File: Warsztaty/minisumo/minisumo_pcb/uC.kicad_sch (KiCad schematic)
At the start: 10 parts, among them U4 ATMEGA328P-AU

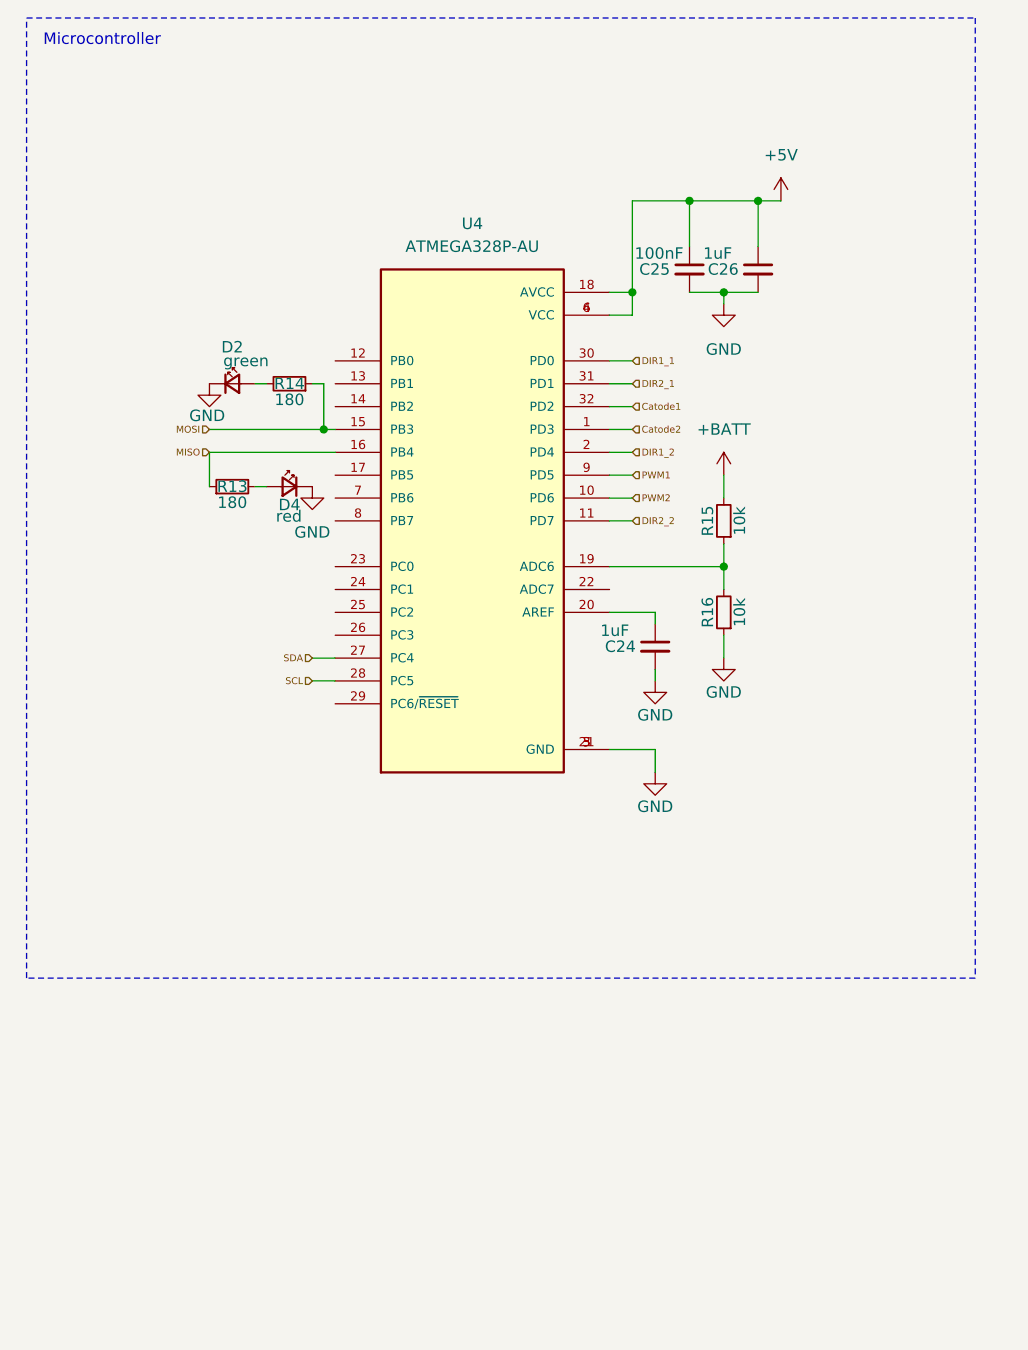
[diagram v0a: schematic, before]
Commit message: laczenie hierarchiczne schematu
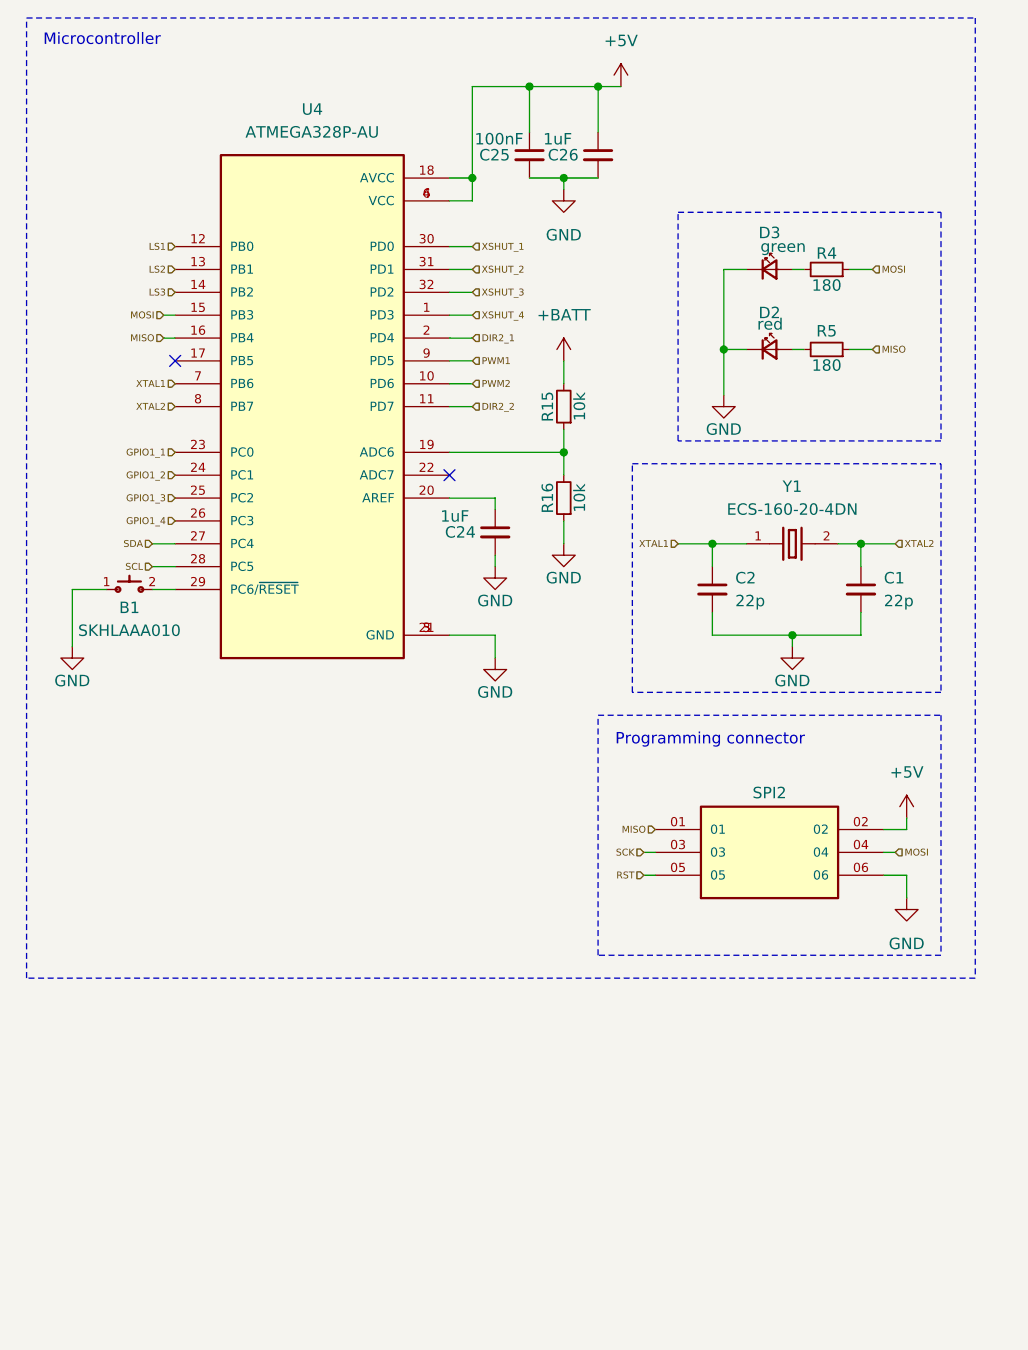
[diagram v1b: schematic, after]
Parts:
- removed D4: red, symbol Device:LED_Small
- removed R13, R14: 180, symbol Device:R_Small
- added B1: SKHLAAA010, SKHLAAA010:SKHLAAA010, symbol SKHLAAA010:SKHLAAA010
- added C1, C2: 22p, symbol Device:C_Small
- added D3: green, symbol Device:LED_Small
- added R4, R5: 180, symbol Device:R_Small
- added SPI2: MTSW-103-23-F-D-230, MTSW-103-23-F-D-230:SAMTEC_MTSW-103-23-F-D-230, symbol MTSW-103-23-F-D-230:MTSW-103-23-F-D-230
- added Y1: ECS-160-20-4DN, ECS-160-20-4DN:XTAL_ECS-160-20-4DN, symbol ECS-160-20-4DN:ECS-160-20-4DN
- D2: value green -> red
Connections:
- net DIR1_2 is gone; now on net DIR2_1: U4.2 (PD4)
- net +5V: now also SPI2.02
- net DIR2_1: no longer U4.31 (PD1)
- net GND: now also B1.1, C1.2, C2.2, D3.1 (K), SPI2.06
- net MISO: now also R5.1, SPI2.01
- net MOSI: now also R4.1, SPI2.04
- net LS1: now reaches U4.12 (PB0)
- net LS2: now reaches U4.13 (PB1)
- net LS3: now reaches U4.14 (PB2)
- net GPIO1_1: now reaches U4.23 (PC0)
- net GPIO1_2: now reaches U4.24 (PC1)
- net GPIO1_3: now reaches U4.25 (PC2)
- net GPIO1_4: now reaches U4.26 (PC3)
- net at U4.29 (PC6/~{RESET}): now also B1.2
- net XTAL1: now reaches U4.7 (PB6)
- net XTAL1: now also C2.1, Y1.1
- net XTAL2: now reaches U4.8 (PB7)
- net XTAL2: now also C1.1, Y1.2
- net at D2.2 (A): now also R5.2
- net Catode1 renamed XSHUT_3
- net Catode2 renamed XSHUT_4
- net DIR1_1 renamed XSHUT_1
- new net: D3.2 (A), R4.2
- new net RST: SPI2.05
- new net SCK: SPI2.03
- new net XSHUT_2: U4.31 (PD1)
- no-connect marks 0 -> 2
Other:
- note added: "Programming connector"
- moved on the sheet: C24, C25, C26, R15, R16, U4

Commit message: wstepnie skonczony schemat
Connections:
- net DIR2_1 renamed DIR1_2
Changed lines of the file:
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@@
 		)
 	)
-	(hierarchical_label "DIR2_1"
+	(hierarchical_label "DIR1_2"
 		(shape input)
 		(at 64.77 50.8 0)

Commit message: chyba gotowy schemat
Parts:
- removed SPI2: MTSW-103-23-F-D-230, MTSW-103-23-F-D-230:SAMTEC_MTSW-103-23-F-D-230, symbol MTSW-103-23-F-D-230:MTSW-103-23-F-D-230
- added SENS1, SENS2, SENS3, SENS4: MTSW-103-23-F-D-230, MTSW-103-23-F-D-230:SAMTEC_MTSW-103-23-F-D-230, symbol MTSW-103-23-F-D-230:MTSW-103-23-F-D-230
- C1, C2, C24, C25, C26: footprint (none) -> Capacitor_SMD:C_0805_2012Metric_Pad1.18x1.45mm_HandSolder
- D2, D3: footprint (none) -> LED_THT:LED_D3.0mm
- R15, R16, R4, R5: footprint (none) -> Resistor_SMD:R_0805_2012Metric_Pad1.20x1.40mm_HandSolder
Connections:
- net GND: now also SENS1.01, SENS2.01, SENS3.01, SENS4.01
- net GPIO1_1: now also SENS1.03
- net GPIO1_2: now also SENS2.03
- net GPIO1_3: now also SENS3.03
- net GPIO1_4: now also SENS4.03
- net SCL: now also SENS1.05, SENS2.05, SENS3.05, SENS4.05
- net SDA: now also SENS1.06, SENS2.06, SENS3.06, SENS4.06
- net XSHUT_1: now also SENS1.04
- net XSHUT_2: now also SENS2.04
- net XSHUT_3: now also SENS3.04
- net XSHUT_4: now also SENS4.04
- new net +3V3: SENS1.02, SENS2.02, SENS3.02, SENS4.02
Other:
- note removed: "Programming connector"

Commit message: chyba gotowy schemat
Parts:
- removed SENS1, SENS2, SENS3, SENS4: MTSW-103-23-F-D-230, MTSW-103-23-F-D-230:SAMTEC_MTSW-103-23-F-D-230, symbol MTSW-103-23-F-D-230:MTSW-103-23-F-D-230
- added C18: 100nF, Capacitor_SMD:C_0805_2012Metric_Pad1.18x1.45mm_HandSolder, symbol Device:C_Small
- added R47: 10k, Resistor_SMD:R_0805_2012Metric_Pad1.20x1.40mm_HandSolder, symbol Device:R_Small
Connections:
- net +5V: now also C18.1, R47.2
- net GND: now also C18.2
- net GPIO1_1: now also U4.12 (PB0); no longer U4.23 (PC0)
- net GPIO1_2: now also U4.13 (PB1); no longer U4.24 (PC1)
- net GPIO1_3: now also U4.14 (PB2); no longer U4.25 (PC2)
- net LS1: now also U4.23 (PC0); no longer U4.12 (PB0)
- net LS2: now also U4.24 (PC1); no longer U4.13 (PB1)
- net LS3: now also U4.25 (PC2); no longer U4.14 (PB2)
- net SCK: now reaches U4.17 (PB5)
- net RST: now reaches B1.2, U4.29 (PC6/~{RESET})
- net RST: now also R47.1
- net DIR1_2 renamed DIRB_1
- net DIR2_2 renamed DIRB_2
- no-connect marks 2 -> 1
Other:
- moved on the sheet: B1, C1, C2, C24, C25, C26, D2, D3, R15, R16, R4, R5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

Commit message: stan przed usunięciem jednego czujnika lini
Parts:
- C1, C18, C2, C24, C25, C26: footprint Capacitor_SMD:C_0805_2012Metric_Pad1.18x1.45mm_HandSolder -> Capacitor_SMD:C_0805_2012Metric
- R15, R16, R4, R5: footprint Resistor_SMD:R_0805_2012Metric_Pad1.20x1.40mm_HandSolder -> Resistor_SMD:R_0805_2012Metric
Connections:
- net LS3: no longer names the net of U4.25 (PC2)
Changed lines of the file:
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@@
-		)
-	)
-	(hierarchical_label "LS3"
-		(shape input)
-		(at 50.8 68.58 180)
-		(fields_autoplaced yes)
-		(effects
-			(font
-				(size 0.762 0.762)
-			)
-			(justify right)
 		)
 	)
@@
 			)
 		)
-		(property "Footprint" "Capacitor_SMD:C_0805_2012Metric_Pad1.18x1.45mm_HandSolder"
+		(property "Footprint" "Capacitor_SMD:C_0805_2012Metric"
 			(at 59.69 107.95 0)
 			(effects
@@
 			)
 		)
-		(property "Footprint" "Resistor_SMD:R_0805_2012Metric_Pad1.20x1.40mm_HandSolder"
+		(property "Footprint" "Resistor_SMD:R_0805_2012Metric"
 			(at 93.98 68.58 0)
 			(effects
@@
 			)
 		)
-		(property "Footprint" "Capacitor_SMD:C_0805_2012Metric_Pad1.18x1.45mm_HandSolder"
+		(property "Footprint" "Capacitor_SMD:C_0805_2012Metric"
 			(at 90.17 30.48 0)
 			(effects
@@
 			)
 		)
-		(property "Footprint" "Resistor_SMD:R_0805_2012Metric_Pad1.20x1.40mm_HandSolder"
+		(property "Footprint" "Resistor_SMD:R_0805_2012Metric"
 			(at 93.98 58.42 0)
 			(effects
@@
 			)
 		)
-		(property "Footprint" "Capacitor_SMD:C_0805_2012Metric_Pad1.18x1.45mm_HandSolder"
+		(property "Footprint" "Capacitor_SMD:C_0805_2012Metric"
 			(at 76.2 107.95 0)
 			(effects
@@
 			)
 		)
-		(property "Footprint" "Capacitor_SMD:C_0805_2012Metric_Pad1.18x1.45mm_HandSolder"
+		(property "Footprint" "Capacitor_SMD:C_0805_2012Metric"
 			(at 97.79 30.48 0)
 			(effects
@@
 			)
 		)
-		(property "Footprint" "Capacitor_SMD:C_0805_2012Metric_Pad1.18x1.45mm_HandSolder"
+		(property "Footprint" "Capacitor_SMD:C_0805_2012Metric"
 			(at 86.36 72.39 0)
 			(effects
@@
 			)
 		)
-		(property "Footprint" "Resistor_SMD:R_0805_2012Metric_Pad1.20x1.40mm_HandSolder"
+		(property "Footprint" "Resistor_SMD:R_0805_2012Metric"
 			(at 34.29 109.22 0)
 			(effects
@@
 			)
 		)
-		(property "Footprint" "Resistor_SMD:R_0805_2012Metric_Pad1.20x1.40mm_HandSolder"
+		(property "Footprint" "Resistor_SMD:R_0805_2012Metric"
 			(at 34.29 100.33 0)
 			(effects
@@
 			)
 		)
-		(property "Footprint" "Capacitor_SMD:C_0805_2012Metric_Pad1.18x1.45mm_HandSolder"
+		(property "Footprint" "Capacitor_SMD:C_0805_2012Metric"
 			(at 31.75 69.85 0)
 			(effects

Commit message: Wstępny wyglad robota i płytki
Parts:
- added J2: MTSW-103-23-F-S-235, MTSW-103-23-F-S-235:SAMTEC_MTSW-103-23-F-S-235, symbol MTSW-103-23-F-S-235:MTSW-103-23-F-S-235
- D2, D3: footprint LED_THT:LED_D3.0mm -> LED_SMD:LED_0805_2012Metric
- R4, R5: value 180 -> 1k
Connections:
- net +5V: now also J2.01
- net GND: now also J2.02
- net LS3: now reaches U4.25 (PC2)
- net GPIO1_1: no longer names the net of U4.12 (PB0)
- net GPIO1_2: no longer names the net of U4.13 (PB1)
- net GPIO1_3: no longer names the net of U4.14 (PB2)
- net GPIO1_4 renamed STARTER
- net STARTER: now also J2.03
- no-connect marks 1 -> 4
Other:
- note added: "Starter connector"

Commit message: koncowy projekt plytki i chyba model tez
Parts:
- renumbered D2 to MISO1, D3 to MOSI1, U4 to uC1
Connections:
- net LS1: now also uC1.25 (PC2); no longer uC1.23 (PC0)
- net LS3: now also uC1.23 (PC0); no longer uC1.25 (PC2)
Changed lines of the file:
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@@
 		)
 	)
-	(hierarchical_label "LS1"
+	(hierarchical_label "LS3"
 		(shape input)
 		(at 50.8 63.5 180)
@@
 		)
 	)
-	(hierarchical_label "LS3"
+	(hierarchical_label "LS1"
 		(shape input)
 		(at 50.8 68.58 180)
@@
 		(dnp no)
 		(fields_autoplaced yes)
-		(property "Reference" "U4"
+		(property "Reference" "uC1"
 			(at 66.04 25.4 0)
 			(effects
@@
 			(project "minisumo_pcb"
 				(path "/7b99a4ad-c15f-48f5-acdf-b2b295c8ee3b/2841fc75-29f5-4e06-b481-1d26a5df72c5"
-					(reference "U4")
+					(reference "uC1")
 					(unit 1)
 				)
@@
 		(on_board yes)
 		(dnp no)
-		(property "Reference" "D3"
+		(property "Reference" "MOSI1"
 			(at 27.94 96.266 0)
 			(effects
@@
 			(project "minisumo_pcb"
 				(path "/7b99a4ad-c15f-48f5-acdf-b2b295c8ee3b/2841fc75-29f5-4e06-b481-1d26a5df72c5"
-					(reference "D3")
+					(reference "MOSI1")
 					(unit 1)
 				)
@@
 		(on_board yes)
 		(dnp no)
-		(property "Reference" "D2"
+		(property "Reference" "MISO1"
 			(at 27.94 105.156 0)
 			(effects
@@
 			(project "minisumo_pcb"
 				(path "/7b99a4ad-c15f-48f5-acdf-b2b295c8ee3b/2841fc75-29f5-4e06-b481-1d26a5df72c5"
-					(reference "D2")
-					(unit 1)
-				)
+					(reference "MISO1")
+					(unit 1)
+				)

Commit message: prawdopodobnie koncowa wersja płytki
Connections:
- net DIRB_2: now also uC1.12 (PB0); no longer uC1.11 (PD7)
- net LS1: now also uC1.23 (PC0); no longer uC1.25 (PC2)
- net LS2: now also uC1.25 (PC2); no longer uC1.24 (PC1)
- net LS3: now also uC1.24 (PC1); no longer uC1.23 (PC0)
- net PWM1: now also uC1.13 (PB1); no longer uC1.9 (PD5)
- net PWM2: now also uC1.14 (PB2); no longer uC1.10 (PD6)
- net XSHUT_1: now also uC1.1 (PD3); no longer uC1.30 (PD0)
- net XSHUT_2: now also uC1.32 (PD2); no longer uC1.31 (PD1)
- net XSHUT_3: now also uC1.31 (PD1); no longer uC1.32 (PD2)
- net XSHUT_4: now also uC1.30 (PD0); no longer uC1.1 (PD3)
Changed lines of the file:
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@@
 	)
 	(no_connect
-		(at 50.8 43.18)
+		(at 83.82 55.88)
 	)
 	(no_connect
-		(at 50.8 45.72)
+		(at 83.82 58.42)
 	)
 	(no_connect
@@
 	)
 	(no_connect
-		(at 50.8 40.64)
+		(at 83.82 53.34)
 	)
 	(wire
@@
 	(wire
 		(pts
+			(xy 49.53 43.18) (xy 50.8 43.18)
+		)
+		(stroke
+			(width 0)
+			(type default)
+		)
+	)
+	(wire
+		(pts
 			(xy 93.98 60.96) (xy 93.98 63.5)
 		)
@@
 	(wire
 		(pts
+			(xy 49.53 45.72) (xy 50.8 45.72)
+		)
+		(stroke
+			(width 0)
+			(type default)
+		)
+	)
+	(wire
+		(pts
 			(xy 81.28 33.02) (xy 83.82 33.02)
 		)
@@
 	(wire
 		(pts
+			(xy 49.53 40.64) (xy 50.8 40.64)
+		)
+		(stroke
+			(width 0)
+			(type default)
+		)
+	)
+	(wire
+		(pts
 			(xy 86.36 68.58) (xy 86.36 69.85)
 		)
@@
 		)
 	)
-	(hierarchical_label "DIRB_2"
+	(hierarchical_label "RST"
 		(shape input)
-		(at 83.82 58.42 0)
+		(at 29.21 78.74 180)
 		(fields_autoplaced yes)
 		(effects
@@
 				(size 0.762 0.762)
 			)
-			(justify left)
+			(justify right)
 		)
 	)
-	(hierarchical_label "RST"
+	(hierarchical_label "XSHUT_4"
 		(shape input)
-		(at 29.21 78.74 180)
+		(at 83.82 40.64 0)
 		(fields_autoplaced yes)
 		(effects
@@
 				(size 0.762 0.762)
 			)
-			(justify right)
+			(justify left)
 		)
 	)
-	(hierarchical_label "LS2"
+	(hierarchical_label "MOSI"
 		(shape input)
-		(at 50.8 66.04 180)
+		(at 39.37 100.33 0)
 		(fields_autoplaced yes)
 		(effects
@@
 				(size 0.762 0.762)
 			)
-			(justify right)
+			(justify left)
 		)
 	)
-	(hierarchical_label "PWM1"
+	(hierarchical_label "XSHUT_2"
 		(shape input)
-		(at 83.82 53.34 0)
+		(at 83.82 45.72 0)
 		(fields_autoplaced yes)
 		(effects
@@
 		)
 	)
-	(hierarchical_label "MOSI"
+	(hierarchical_label "SCK"
 		(shape input)
-		(at 39.37 100.33 0)
+		(at 50.8 53.34 180)
 		(fields_autoplaced yes)
 		(effects
@@
 				(size 0.762 0.762)
 			)
-			(justify left)
+			(justify right)
 		)
 	)
-	(hierarchical_label "XSHUT_3"
+	(hierarchical_label "MISO"
 		(shape input)
-		(at 83.82 45.72 0)
+		(at 39.37 109.22 0)
 		(fields_autoplaced yes)
 		(effects
@@
 		)
 	)
-	(hierarchical_label "PWM2"
+	(hierarchical_label "XSHUT_1"
 		(shape input)
-		(at 83.82 55.88 0)
+		(at 83.82 48.26 0)
 		(fields_autoplaced yes)
 		(effects
@@
 		)
 	)
-	(hierarchical_label "SCK"
+	(hierarchical_label "PWM2"
 		(shape input)
-		(at 50.8 53.34 180)
+		(at 49.53 45.72 180)
 		(fields_autoplaced yes)
 		(effects
@@
 		)
 	)
-	(hierarchical_label "MISO"
+	(hierarchical_label "MOSI"
 		(shape input)
-		(at 39.37 109.22 0)
+		(at 49.53 48.26 180)
 		(fields_autoplaced yes)
 		(effects
@@
 				(size 0.762 0.762)
 			)
-			(justify left)
+			(justify right)
 		)
 	)
-	(hierarchical_label "MOSI"
+	(hierarchical_label "LS3"
 		(shape input)
-		(at 49.53 48.26 180)
+		(at 50.8 66.04 180)
 		(fields_autoplaced yes)
 		(effects
@@
 		)
 	)
-	(hierarchical_label "LS3"
+	(hierarchical_label "LS2"
 		(shape input)
-		(at 50.8 63.5 180)
+		(at 50.8 68.58 180)
 		(fields_autoplaced yes)
 		(effects
@@
 		)
 	)
-	(hierarchical_label "SDA"
+	(hierarchical_label "DIRB_2"
 		(shape input)
-		(at 48.26 73.66 180)
+		(at 49.53 40.64 180)
 		(fields_autoplaced yes)
 		(effects
@@
 		)
 	)
-	(hierarchical_label "LS1"
+	(hierarchical_label "SDA"
 		(shape input)
-		(at 50.8 68.58 180)
+		(at 48.26 73.66 180)
 		(fields_autoplaced yes)
 		(effects
@@
 		)
 	)
-	(hierarchical_label "XSHUT_4"
+	(hierarchical_label "LS1"
 		(shape input)
-		(at 83.82 48.26 0)
+		(at 50.8 63.5 180)
 		(fields_autoplaced yes)
 		(effects
@@
 				(size 0.762 0.762)
 			)
-			(justify left)
+			(justify right)
 		)
 	)
-	(hierarchical_label "DIRB_1"
+	(hierarchical_label "PWM1"
 		(shape input)
-		(at 83.82 50.8 0)
+		(at 49.53 43.18 180)
 		(fields_autoplaced yes)
 		(effects
@@
 				(size 0.762 0.762)
 			)
-			(justify left)
+			(justify right)
 		)
 	)
-	(hierarchical_label "XSHUT_1"
+	(hierarchical_label "DIRB_1"
 		(shape input)
-		(at 83.82 40.64 0)
+		(at 83.82 50.8 0)
 		(fields_autoplaced yes)
 		(effects
@@
 		)
 	)
-	(hierarchical_label "XSHUT_2"
+	(hierarchical_label "XSHUT_3"
 		(shape input)
 		(at 83.82 43.18 0)
@@
 		(lib_id "Device:C_Small")
 		(at 31.75 69.85 0)
+		(mirror y)
 		(unit 1)
 		(exclude_from_sim no)
@@
 		(dnp no)
 		(property "Reference" "C18"
-			(at 26.162 69.85 0)
+			(at 37.338 69.85 0)
 			(effects
 				(font
@@
 		)
 		(property "Value" "100nF"
-			(at 25.654 68.072 0)
+			(at 37.846 68.072 0)
 			(effects
 				(font
